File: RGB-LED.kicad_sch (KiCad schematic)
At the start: 5 parts

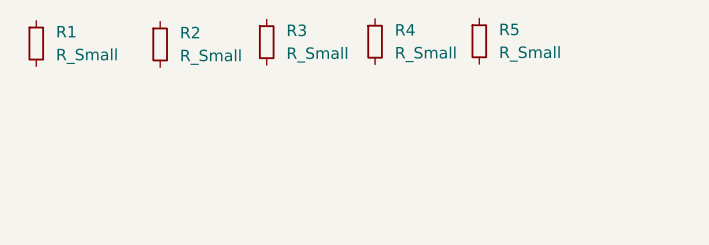
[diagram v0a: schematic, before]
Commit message: Added two capacitors.
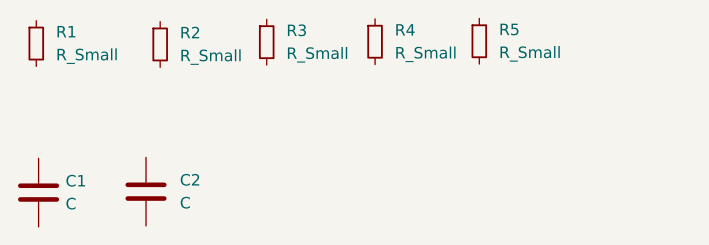
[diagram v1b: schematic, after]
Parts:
- added C1, C2: C, symbol Device:C
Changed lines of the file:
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@@
+    (pin "2")
+  )
+  (symbol (lib_id "Device:C") (at 49.5808 93.0656 0) (unit 1)
+    (in_bom yes) (on_board yes) (fields_autoplaced)
+    (property "Reference" "C2" (id 0) (at 53.34 91.7955 0)
+      (effects (font (size 1.27 1.27)) (justify left))
+    )
+    (property "Value" "C" (id 1) (at 53.34 94.3355 0)
+      (effects (font (size 1.27 1.27)) (justify left))
+    )
+    (property "Footprint" "" (id 2) (at 50.546 96.8756 0)
+      (effects (font (size 1.27 1.27)) hide)
+    )
+    (property "Datasheet" "~" (id 3) (at 49.5808 93.0656 0)
+      (effects (font (size 1.27 1.27)) hide)
+    )
+    (pin "1")
+    (pin "2")
+  )
+  (symbol (lib_id "Device:C") (at 37.6428 93.1672 0) (unit 1)
+    (in_bom yes) (on_board yes) (fields_autoplaced)
+    (property "Reference" "C1" (id 0) (at 40.64 91.8971 0)
+      (effects (font (size 1.27 1.27)) (justify left))
+    )
+    (property "Value" "C" (id 1) (at 40.64 94.4371 0)
+      (effects (font (size 1.27 1.27)) (justify left))
+    )
+    (property "Footprint" "" (id 2) (at 38.608 96.9772 0)
+      (effects (font (size 1.27 1.27)) hide)
+    )
+    (property "Datasheet" "~" (id 3) (at 37.6428 93.1672 0)
+      (effects (font (size 1.27 1.27)) hide)
+    )
+    (pin "1")
     (pin "2")
   )
@@
   )
   (symbol_instances
+    (path "/df3464cb-aae1-46f5-82f8-c08a4aa396a0"
+      (reference "C1") (unit 1) (value "C") (footprint "")
+    )
+    (path "/ded3d56b-fc99-4e83-9ce2-73d0cdc9ba59"
+      (reference "C2") (unit 1) (value "C") (footprint "")
+    )
     (path "/10460aa8-9785-4798-bcc4-28fad2b5f163"
       (reference "R1") (unit 1) (value "R_Small") (footprint "")

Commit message: Added R6
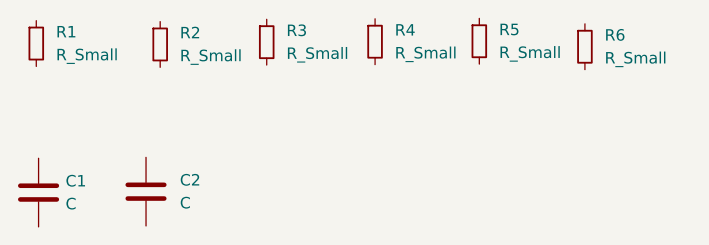
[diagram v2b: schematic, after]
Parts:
- added R6: R_Small, symbol Device:R_Small
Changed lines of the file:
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@@
+    (pin "2")
+  )
+  (symbol (lib_id "Device:R_Small") (at 98.3488 76.962 0) (unit 1)
+    (in_bom yes) (on_board yes) (fields_autoplaced)
+    (property "Reference" "R6" (id 0) (at 100.5332 75.6919 0)
+      (effects (font (size 1.27 1.27)) (justify left))
+    )
+    (property "Value" "R_Small" (id 1) (at 100.5332 78.2319 0)
+      (effects (font (size 1.27 1.27)) (justify left))
+    )
+    (property "Footprint" "" (id 2) (at 98.3488 76.962 0)
+      (effects (font (size 1.27 1.27)) hide)
+    )
+    (property "Datasheet" "~" (id 3) (at 98.3488 76.962 0)
+      (effects (font (size 1.27 1.27)) hide)
+    )
+    (pin "1")
     (pin "2")
   )
@@
       (reference "R5") (unit 1) (value "R_Small") (footprint "")
     )
+    (path "/c0534892-950c-45f8-810f-c53af5e020c2"
+      (reference "R6") (unit 1) (value "R_Small") (footprint "")
+    )
   )
